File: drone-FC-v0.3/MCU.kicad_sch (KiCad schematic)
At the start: 11 parts, among them J11 USB_C_Receptacle_USB2.0_16P, U2 ESP32-S3-WROOM-1

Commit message: "global labels added"
"global labels added"
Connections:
- net GPIO4 renamed GPIO 4
- net GPIO5 renamed GPIO 5
- net GPIO6 renamed GPIO 6
- net GPIO7 renamed GPIO 7
- net GPIO8 renamed GPIO 8
- net Low_chip_selected: no longer names the net of U2.17 (IO9)

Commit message: added global labels for BMI088
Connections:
- net MOSI: now reaches U2.16 (IO46)
- net CSB_GYRO: now reaches U2.17 (IO9)
- net MISO: now reaches U2.35 (IO42)
- net GPIO15: now reaches U2.8 (IO15)
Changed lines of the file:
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@@
 	(wire
 		(pts
-			(xy 193.04 71.12) (xy 210.82 71.12)
+			(xy 201.93 71.12) (xy 210.82 71.12)
 		)
 		(stroke
@@
 		)
 	)
+	(global_label "GPIO15"
+		(shape input)
+		(at 210.82 86.36 180)
+		(fields_autoplaced yes)
+		(effects
+			(font
+				(size 1.27 1.27)
+			)
+			(justify right)
+		)
+		(property "Intersheetrefs" "${INTERSHEET_REFS}"
+			(at 200.9405 86.36 0)
+			(hide yes)
+			(show_name no)
+			(do_not_autoplace no)
+			(effects
+				(font
+					(size 1.27 1.27)
+				)
+				(justify right)
+			)
+		)
+	)
 	(global_label "GPIO 7"
 		(shape input)
@@
 		)
 	)
+	(global_label "MOSI"
+		(shape input)
+		(at 241.3 83.82 0)
+		(fields_autoplaced yes)
+		(effects
+			(font
+				(size 1.27 1.27)
+			)
+			(justify left)
+		)
+		(property "Intersheetrefs" "${INTERSHEET_REFS}"
+			(at 248.8814 83.82 0)
+			(hide yes)
+			(show_name no)
+			(do_not_autoplace no)
+			(effects
+				(font
+					(size 1.27 1.27)
+				)
+				(justify left)
+			)
+		)
+	)
 	(global_label "SDA_MAG"
 		(shape input)
@@
 			(hide yes)
 			(show_name no)
+			(do_not_autoplace no)
+			(effects
+				(font
+					(size 1.27 1.27)
+				)
+				(justify right)
+			)
+		)
+	)
+	(global_label "MISO"
+		(shape input)
+		(at 241.3 78.74 0)
+		(fields_autoplaced yes)
+		(effects
+			(font
+				(size 1.27 1.27)
+			)
+			(justify left)
+		)
+		(property "Intersheetrefs" "${INTERSHEET_REFS}"
+			(at 248.8814 78.74 0)
+			(hide yes)
+			(show_name no)
+			(do_not_autoplace no)
+			(effects
+				(font
+					(size 1.27 1.27)
+				)
+				(justify left)
+			)
+		)
+	)
+	(global_label "CSB_GYRO"
+		(shape input)
+		(at 201.93 71.12 180)
+		(fields_autoplaced yes)
+		(effects
+			(font
+				(size 1.27 1.27)
+			)
+			(justify right)
+		)
+		(property "Intersheetrefs" "${INTERSHEET_REFS}"
+			(at 189.2686 71.12 0)
+			(hide yes)
+			(show_name no)

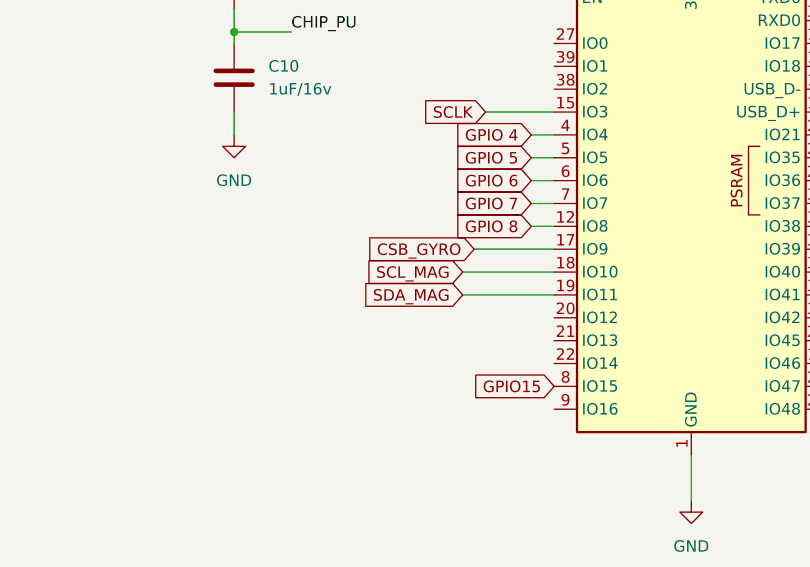
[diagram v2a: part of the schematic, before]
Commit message: added sda and scl labels
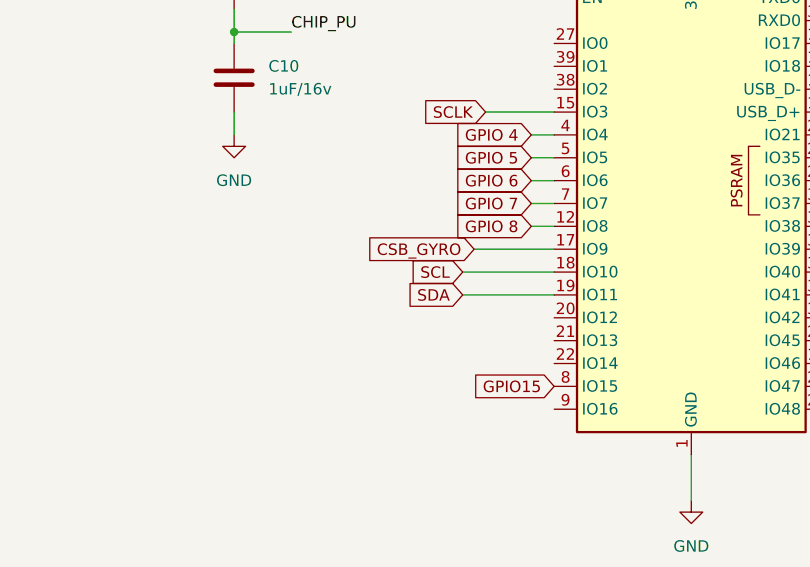
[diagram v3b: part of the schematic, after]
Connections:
- net SCL_MAG renamed SCL
- net SDA_MAG renamed SDA
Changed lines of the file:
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@@
 		)
 	)
-	(global_label "SDA_MAG"
+	(global_label "SDA"
 		(shape input)
 		(at 200.66 76.2 180)
@@
 		)
 		(property "Intersheetrefs" "${INTERSHEET_REFS}"
-			(at 189.3291 76.2 0)
+			(at 194.1067 76.2 0)
 			(hide yes)
 			(show_name no)
@@
 		)
 	)
-	(global_label "SCL_MAG"
+	(global_label "SCL"
 		(shape input)
 		(at 200.66 73.66 180)
@@
 		)
 		(property "Intersheetrefs" "${INTERSHEET_REFS}"
-			(at 189.3896 73.66 0)
+			(at 194.1672 73.66 0)
 			(hide yes)
 			(show_name no)

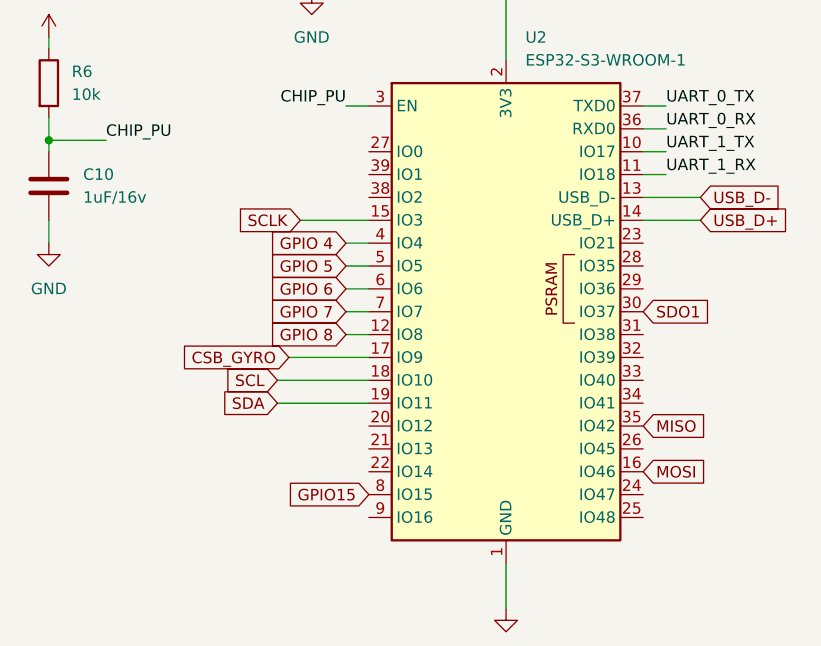
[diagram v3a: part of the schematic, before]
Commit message: added connections and ground plane
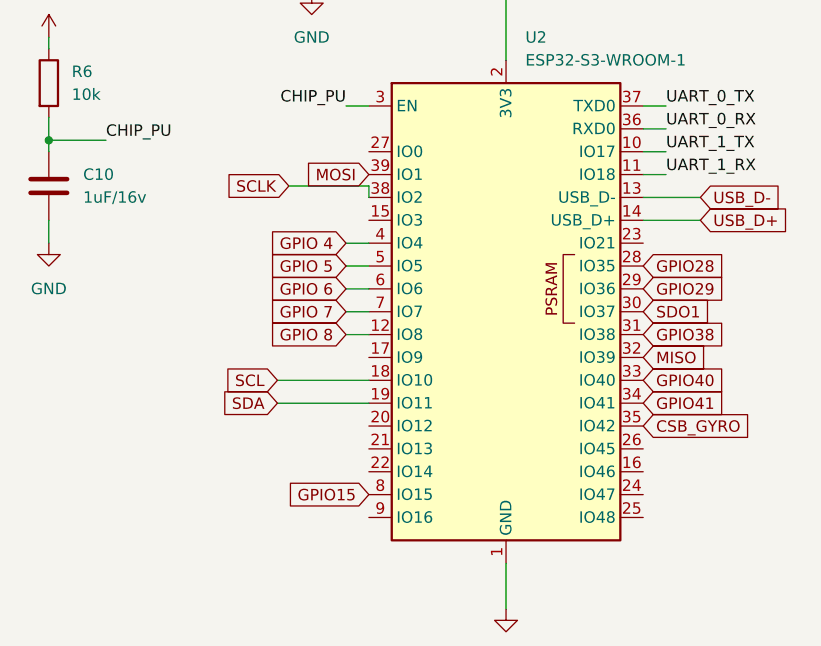
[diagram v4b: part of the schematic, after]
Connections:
- net CSB_GYRO: now also U2.35 (IO42); no longer U2.17 (IO9)
- net MISO: now also U2.32 (IO39); no longer U2.35 (IO42)
- net MOSI: now also U2.39 (IO1); no longer U2.16 (IO46)
- net SCLK: now also U2.38 (IO2); no longer U2.15 (IO3)
- net GPIO28: now reaches U2.28 (IO35)
- net GPIO29: now reaches U2.29 (IO36)
- net GPIO38: now reaches U2.31 (IO38)
- net GPIO40: now reaches U2.33 (IO40)
- net GPIO41: now reaches U2.34 (IO41)
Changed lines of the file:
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@@
+	(wire
+		(pts
+			(xy 201.93 52.07) (xy 210.82 52.07)
+		)
+		(stroke
+			(width 0)
+			(type default)
+		)
+	)
 	(wire
 		(pts
@@
 	(wire
 		(pts
-			(xy 203.2 55.88) (xy 210.82 55.88)
-		)
-		(stroke
-			(width 0)
-			(type default)
-		)
-	)
-	(wire
-		(pts
 			(xy 198.12 29.21) (xy 204.47 29.21)
 		)
@@
 	(wire
 		(pts
-			(xy 201.93 71.12) (xy 210.82 71.12)
+			(xy 210.82 52.07) (xy 210.82 53.34)
 		)
 		(stroke
@@
 		)
 	)
+	(global_label "MISO"
+		(shape input)
+		(at 241.3 71.12 0)
+		(fields_autoplaced yes)
+		(effects
+			(font
+				(size 1.27 1.27)
+			)
+			(justify left)
+		)
+		(property "Intersheetrefs" "${INTERSHEET_REFS}"
+			(at 248.8814 71.12 0)
+			(hide yes)
+			(show_name no)
+			(do_not_autoplace no)
+			(effects
+				(font
+					(size 1.27 1.27)
+				)
+				(justify left)
+			)
+		)
+	)
 	(global_label "GPIO 4"
 		(shape input)
@@
 		)
 	)
+	(global_label "GPIO38"
+		(shape input)
+		(at 241.3 68.58 0)
+		(fields_autoplaced yes)
+		(effects
+			(font
+				(size 1.27 1.27)
+			)
+			(justify left)
+		)
+		(property "Intersheetrefs" "${INTERSHEET_REFS}"
+			(at 251.1795 68.58 0)
+			(hide yes)
+			(show_name no)
+			(do_not_autoplace no)
+			(effects
+				(font
+					(size 1.27 1.27)
+				)
+				(justify left)
+			)
+		)
+	)
 	(global_label "USB_D+"
 		(shape input)
@@
 	(global_label "MOSI"
 		(shape input)
-		(at 241.3 83.82 0)
-		(fields_autoplaced yes)
-		(effects
-			(font
-				(size 1.27 1.27)
-			)
-			(justify left)
-		)
-		(property "Intersheetrefs" "${INTERSHEET_REFS}"
-			(at 248.8814 83.82 0)
-			(hide yes)
-			(show_name no)
-			(do_not_autoplace no)
-			(effects
-				(font
-					(size 1.27 1.27)
-				)
-				(justify left)
+		(at 210.82 50.8 180)
+		(fields_autoplaced yes)
+		(effects
+			(font
+				(size 1.27 1.27)
+			)
+			(justify right)
+		)
+		(property "Intersheetrefs" "${INTERSHEET_REFS}"
+			(at 203.2386 50.8 0)
+			(hide yes)
+			(show_name no)
+			(do_not_autoplace no)
+			(effects
+				(font
+					(size 1.27 1.27)
+				)
+				(justify right)
 			)
 		)
@@
 		)
 	)
-	(global_label "MISO"
+	(global_label "CSB_GYRO"
 		(shape input)
 		(at 241.3 78.74 0)
@@
 		)
 		(property "Intersheetrefs" "${INTERSHEET_REFS}"
-			(at 248.8814 78.74 0)
-			(hide yes)
-			(show_name no)
-			(do_not_autoplace no)
-			(effects
-				(font
-					(size 1.27 1.27)
-				)
-				(justify left)
-			)
-		)
-	)
-	(global_label "CSB_GYRO"
-		(shape input)
-		(at 201.93 71.12 180)
+			(at 253.9614 78.74 0)
+			(hide yes)
+			(show_name no)
+			(do_not_autoplace no)
+			(effects
+				(font
+					(size 1.27 1.27)
+				)
+				(justify left)
+			)
+		)
+	)
+	(global_label "GPIO 5"
+		(shape input)
+		(at 208.28 60.96 180)
 		(fields_autoplaced yes)
 		(effects
@@
 		)
 		(property "Intersheetrefs" "${INTERSHEET_REFS}"
-			(at 189.2686 71.12 0)
+			(at 198.6424 60.96 0)
 			(hide yes)
 			(show_name no)
@@
 		)
 	)
-	(global_label "GPIO 5"
-		(shape input)
-		(at 208.28 60.96 180)
+	(global_label "SCL"
+		(shape input)
+		(at 200.66 73.66 180)
 		(fields_autoplaced yes)
 		(effects
@@
 		)
 		(property "Intersheetrefs" "${INTERSHEET_REFS}"
-			(at 198.6424 60.96 0)
+			(at 194.1672 73.66 0)
 			(hide yes)
 			(show_name no)
@@
 		)
 	)
-	(global_label "SCL"
-		(shape input)
-		(at 200.66 73.66 180)
+	(global_label "GPIO40"
+		(shape input)
+		(at 241.3 73.66 0)
+		(fields_autoplaced yes)
+		(effects
+			(font
+				(size 1.27 1.27)
+			)
+			(justify left)
+		)
+		(property "Intersheetrefs" "${INTERSHEET_REFS}"
+			(at 251.1795 73.66 0)
+			(hide yes)
+			(show_name no)
+			(do_not_autoplace no)
+			(effects
+				(font
+					(size 1.27 1.27)
+				)
+				(justify left)
+			)
+		)
+	)
+	(global_label "USB_D+"
+		(shape input)
+		(at 111.76 45.72 0)
+		(fields_autoplaced yes)
+		(effects
+			(font
+				(size 1.27 1.27)
+			)
+			(justify left)
+		)
+		(property "Intersheetrefs" "${INTERSHEET_REFS}"
+			(at 122.3652 45.72 0)
+			(hide yes)
+			(show_name no)
+			(do_not_autoplace no)
+			(effects
+				(font
+					(size 1.27 1.27)
+				)
+				(justify left)
+			)
+		)
+	)
+	(global_label "GPIO 8"
+		(shape input)
+		(at 208.28 68.58 180)
 		(fields_autoplaced yes)
 		(effects
@@
 		)
 		(property "Intersheetrefs" "${INTERSHEET_REFS}"
-			(at 194.1672 73.66 0)
+			(at 198.6424 68.58 0)
 			(hide yes)
 			(show_name no)
@@
 		)
 	)
-	(global_label "USB_D+"
-		(shape input)
-		(at 111.76 45.72 0)
-		(fields_autoplaced yes)
-		(effects
-			(font
-				(size 1.27 1.27)
-			)
-			(justify left)
-		)
-		(property "Intersheetrefs" "${INTERSHEET_REFS}"
-			(at 122.3652 45.72 0)
-			(hide yes)
-			(show_name no)
-			(do_not_autoplace no)
-			(effects
-				(font
-					(size 1.27 1.27)
-				)
-				(justify left)
-			)
-		)
-	)
-	(global_label "GPIO 8"
-		(shape input)
-		(at 208.28 68.58 180)
+	(global_label "SDO1"
+		(shape input)
+		(at 241.3 66.04 0)
+		(fields_autoplaced yes)
+		(effects
+			(font
+				(size 1.27 1.27)
+			)
+			(justify left)
+		)
+		(property "Intersheetrefs" "${INTERSHEET_REFS}"
+			(at 249.3047 66.04 0)
+			(hide yes)
+			(show_name no)
+			(do_not_autoplace no)
+			(effects
+				(font
+					(size 1.27 1.27)
+				)
+				(justify left)
+			)
+		)
+	)
+	(global_label "GPIO 6"
+		(shape input)
+		(at 208.28 63.5 180)
 		(fields_autoplaced yes)
 		(effects
@@
 		)
 		(property "Intersheetrefs" "${INTERSHEET_REFS}"
-			(at 198.6424 68.58 0)
+			(at 198.6424 63.5 0)
 			(hide yes)
 			(show_name no)
@@
 		)
 	)
-	(global_label "SDO1"
-		(shape input)
-		(at 241.3 66.04 0)
-		(fields_autoplaced yes)
-		(effects
-			(font
-				(size 1.27 1.27)
-			)
-			(justify left)
-		)
-		(property "Intersheetrefs" "${INTERSHEET_REFS}"
-			(at 249.3047 66.04 0)
-			(hide yes)
-			(show_name no)
-			(do_not_autoplace no)
-			(effects
-				(font
-					(size 1.27 1.27)
-				)
-				(justify left)
-			)
-		)
-	)
-	(global_label "GPIO 6"
-		(shape input)
-		(at 208.28 63.5 180)
+	(global_label "GPIO41"
+		(shape input)
+		(at 241.3 76.2 0)
+		(fields_autoplaced yes)
+		(effects
+			(font
+				(size 1.27 1.27)
+			)
+			(justify left)
+		)
+		(property "Intersheetrefs" "${INTERSHEET_REFS}"
+			(at 251.1795 76.2 0)
+			(hide yes)
+			(show_name no)
+			(do_not_autoplace no)
+			(effects
+				(font
+					(size 1.27 1.27)
+				)
+				(justify left)
+			)
+		)
+	)
+	(global_label "SCLK"
+		(shape input)
+		(at 201.93 52.07 180)
 		(fields_autoplaced yes)
 		(effects
@@
 		)
 		(property "Intersheetrefs" "${INTERSHEET_REFS}"
-			(at 198.6424 63.5 0)
+			(at 194.1672 52.07 0)
 			(hide yes)
 			(show_name no)
@@
 		)
 	)
-	(global_label "SCLK"
-		(shape input)
-		(at 203.2 55.88 180)
-		(fields_autoplaced yes)
-		(effects
-			(font
-				(size 1.27 1.27)
-			)
-			(justify right)
-		)
-		(property "Intersheetrefs" "${INTERSHEET_REFS}"
-			(at 195.4372 55.88 0)
-			(hide yes)
-			(show_name no)
-			(do_not_autoplace no)
-			(effects
-				(font
-					(size 1.27 1.27)
-				)
-				(justify right)
-			)
-		)
+	(global_label "GPIO29"
+		(shape input)
+		(at 241.3 63.5 0)
+		(fields_autoplaced yes)
+		(effects
+			(font
+				(size 1.27 1.27)
+			)
+			(justify left)
+		)
+		(property "Intersheetrefs" "${INTERSHEET_REFS}"
+			(at 251.1795 63.5 0)
+			(hide yes)
+			(show_name no)
+			(do_not_autoplace no)
+			(effects
+				(font
+					(size 1.27 1.27)
+				)
+				(justify left)
+			)
+		)
+	)
+	(global_label "GPIO28"
+		(shape input)
+		(at 241.3 60.96 0)
+		(fields_autoplaced yes)
+		(effects
+			(font
+				(size 1.27 1.27)
+			)
+			(justify left)
+		)
+		(property "Intersheetrefs" "${INTERSHEET_REFS}"
+			(at 251.1795 60.96 0)
+			(hide yes)
+			(show_name no)
+			(do_not_autoplace no)
+			(effects
+				(font
+					(size 1.27 1.27)
+				)
+				(justify left)
+			)
+		)
